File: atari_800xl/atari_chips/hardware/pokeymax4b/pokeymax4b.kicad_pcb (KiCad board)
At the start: 4 copper layers, 20.2 x 52.5 mm, 51 parts, among them J1 Conn_02x02_Odd_Even, J2 Conn_02x03_Odd_Even, J3 Conn_02x05_Odd_Even, U1 TSV854IQ4T, U2 SN74CB3T16211DGVR, U4 SN74CB3T16211DGVR, Y1 ASE-49.152MHz

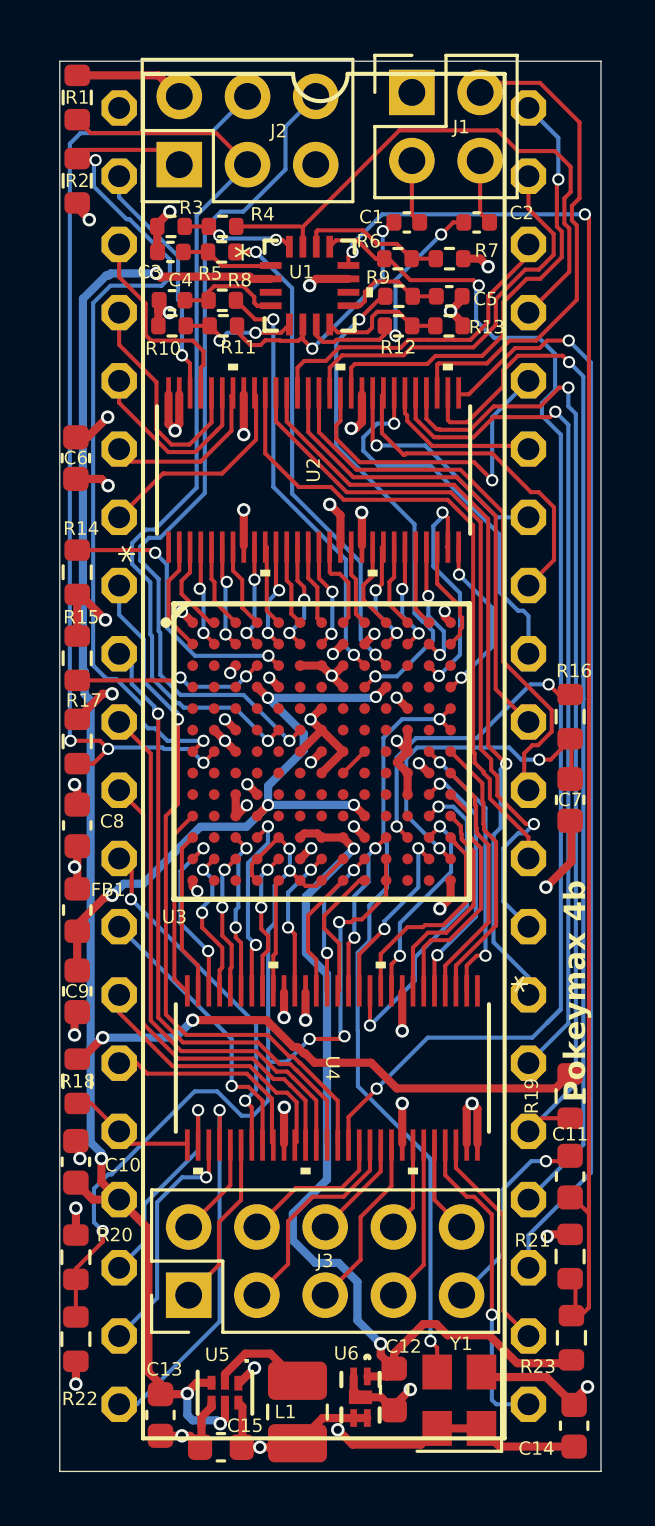
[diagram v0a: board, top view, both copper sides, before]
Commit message: After testing 4b first run, there are a few issues. Updated to 4b2 with: Corrected L/R output. ADC bias improvement. ADC preamp out/in- corrected. Moved silkscreen name!
git-svn-id: svn+ssh://192.168.0.3/home/svnfpga/repo/trunk@1475 d6161ac3-aae1-4d52-9b05-ea9ac36b53d3
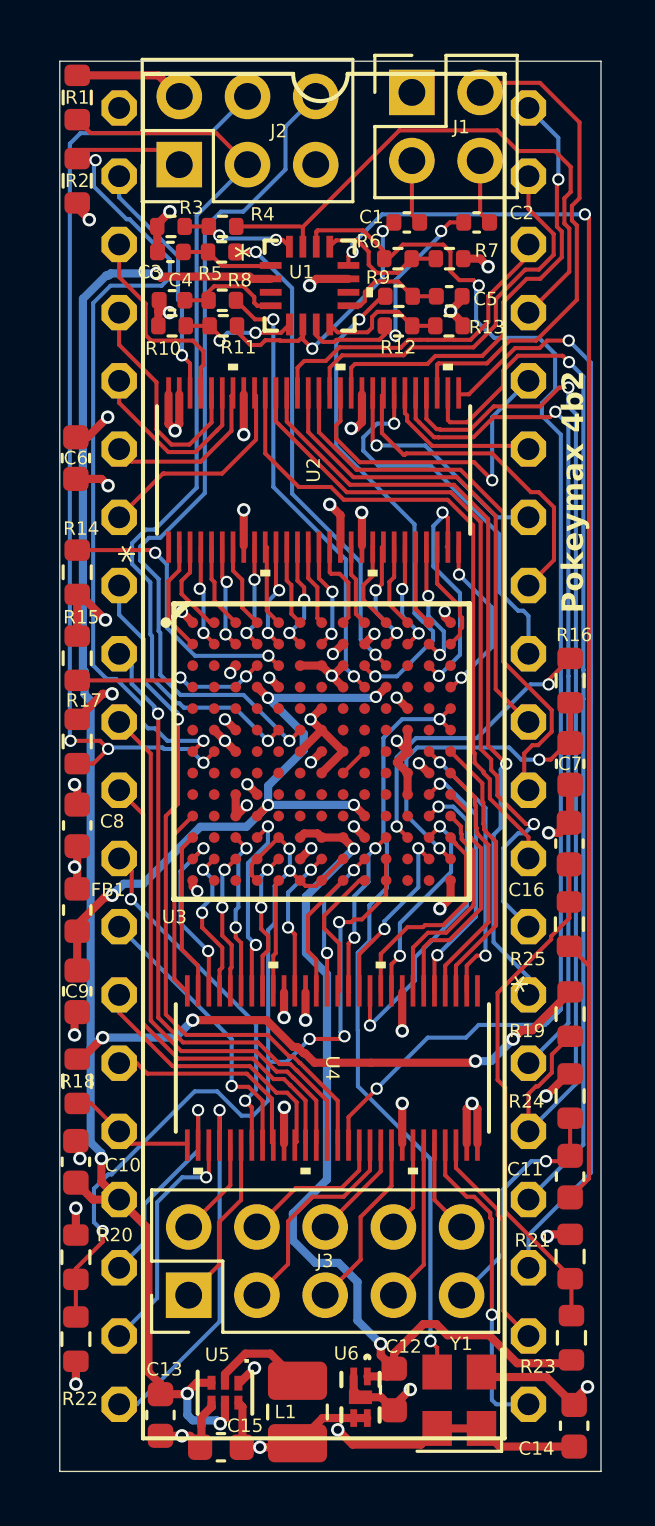
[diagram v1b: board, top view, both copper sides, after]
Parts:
- added C16: 10uF, Capacitor_SMD:C_0603_1608Metric, F.Cu at (36.5, 49.3)
- added R24: 10k, Resistor_SMD:R_0603_1608Metric, F.Cu at (36.5, 58.7)
- added R25: 10k, Resistor_SMD:R_0603_1608Metric, F.Cu at (36.5, 52.3)
- C3, C4, C5: value C -> 18n
- R18, R19: value 2k7 -> DNP
- R21: value 3k3 -> 10k
- R23: value 3k3 -> 110k
- R5, R8, R9: value R -> 560
- U5: value ~ -> 3.3v TPS62237
- U6: value ~ -> MIC94310 2.5v
- moved R19 3.05 mm to (36.5, 55.7)
- moved C7 1.34 mm to (36.5, 46.4)
- moved R16 1.34 mm to (36.5, 43.3)
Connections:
- R21 pad 1: /ADC/AUD_IN_BIAS -> Net-(C16-Pad2)
- R23 pad 2: /ADC/AUD_IN_BIAS -> Net-(C16-Pad2)
- R6 pad 2: Net-(U1-OUT) -> Net-(U1-IN4-)
- R7 pad 1: Net-(U1-OUT) -> Net-(U1-IN4-)
- U1 pad 13: /Audio output/AUD_IN_AMP -> Net-(U1-IN4-)
- U1 pad 14: Net-(U1-OUT) -> /Audio output/AUD_IN_AMP
- U3 pad C9: /Audio output/AUDL -> /Audio output/AUDR
- U3 pad D9: /Audio output/AUDR -> /Audio output/AUDL
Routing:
- net Net-(C16-Pad2): track 0.00 -> 19.5 mm
- net /ADC/AUD_IN_BIAS: track 53.9 -> 48.0 mm
- net Net-(U1-OUT): track 5.47 -> 0.00 mm
- net Net-(U1-IN4-): track 0.00 -> 5.05 mm
- net /Level shifter/LOUT1.B21: track 37.3 -> 39.8 mm
- net /Audio output/AUD_IN_AMP: track 47.3 -> 49.5 mm
- net /ADC/AUD_IN: track 7.62 -> 9.02 mm
- net /ADC/ADC_RX: track 12.8 -> 14.1 mm
- net /Audio output/AUDL: track 16.0 -> 16.8 mm
- net +5V: track 77.3 -> 77.8 mm, vias 6 -> 8
- net GND: track 54.7 -> 55.0 mm, vias 41 -> 42
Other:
- board text added: "Pokeymax 4b2"
- board text removed: "Pokeymax 4b"
